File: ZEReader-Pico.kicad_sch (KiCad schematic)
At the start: 0 parts

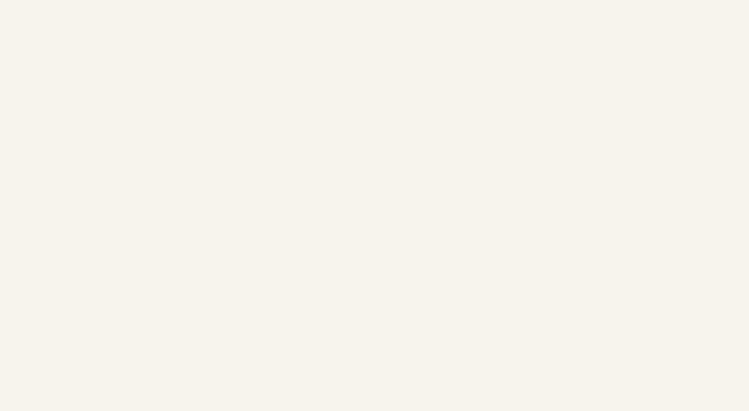
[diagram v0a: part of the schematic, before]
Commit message: Adds SD card connector, control buttons and debug headers
Signed-off-by: Anna-Lena Marx <anna-lena.marx@web.de>
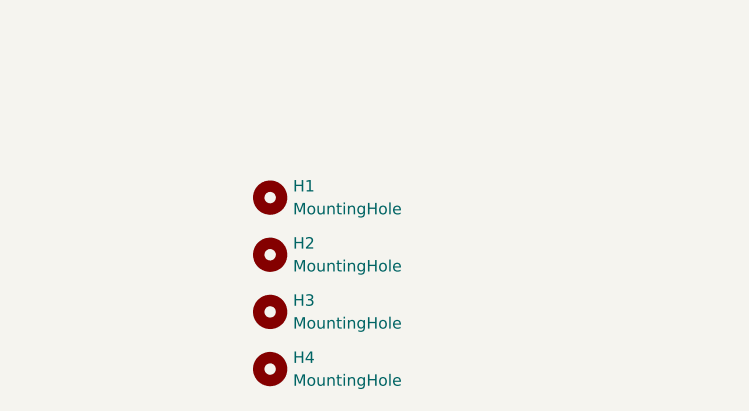
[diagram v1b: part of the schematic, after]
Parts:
- added H1, H2, H3, H4: MountingHole, MountingHole:MountingHole_3.2mm_M3, symbol Mechanical:MountingHole

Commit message: Add EPD Driver Circuit
Signed-off-by: Anna-Lena Marx <anna-lena.marx@web.de>
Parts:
- H1, H2, H3, H4: footprint MountingHole:MountingHole_3.2mm_M3 -> MountingHole:MountingHole_3.2mm_M3_Pad_Via
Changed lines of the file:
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@@
 			)
 		)
-		(property "Footprint" "MountingHole:MountingHole_3.2mm_M3"
+		(property "Footprint" "MountingHole:MountingHole_3.2mm_M3_Pad_Via"
 			(at 78.74 129.54 0)
 			(effects
@@
 			)
 		)
-		(property "Footprint" "MountingHole:MountingHole_3.2mm_M3"
+		(property "Footprint" "MountingHole:MountingHole_3.2mm_M3_Pad_Via"
 			(at 78.74 148.59 0)
 			(effects
@@
 			)
 		)
-		(property "Footprint" "MountingHole:MountingHole_3.2mm_M3"
+		(property "Footprint" "MountingHole:MountingHole_3.2mm_M3_Pad_Via"
 			(at 78.74 142.24 0)
 			(effects
@@
 			)
 		)
-		(property "Footprint" "MountingHole:MountingHole_3.2mm_M3"
+		(property "Footprint" "MountingHole:MountingHole_3.2mm_M3_Pad_Via"
 			(at 78.74 135.89 0)
 			(effects

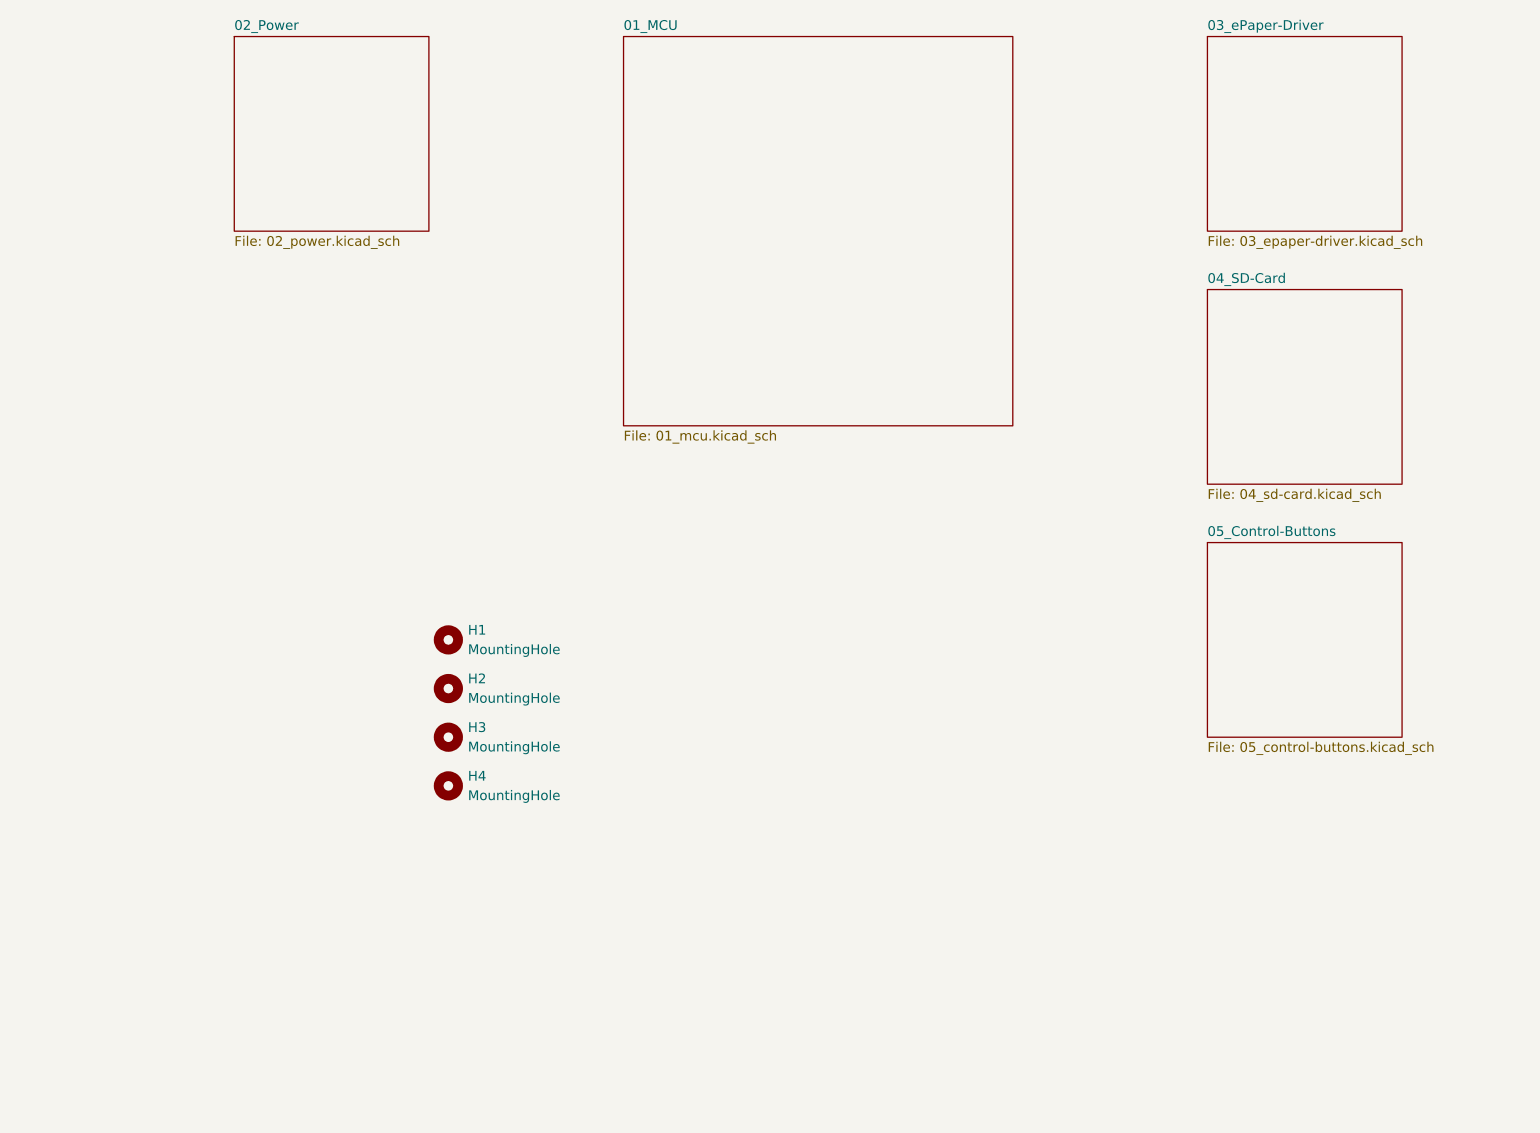
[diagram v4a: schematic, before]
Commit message: Migrate to KiCad 9, start working on the new revision
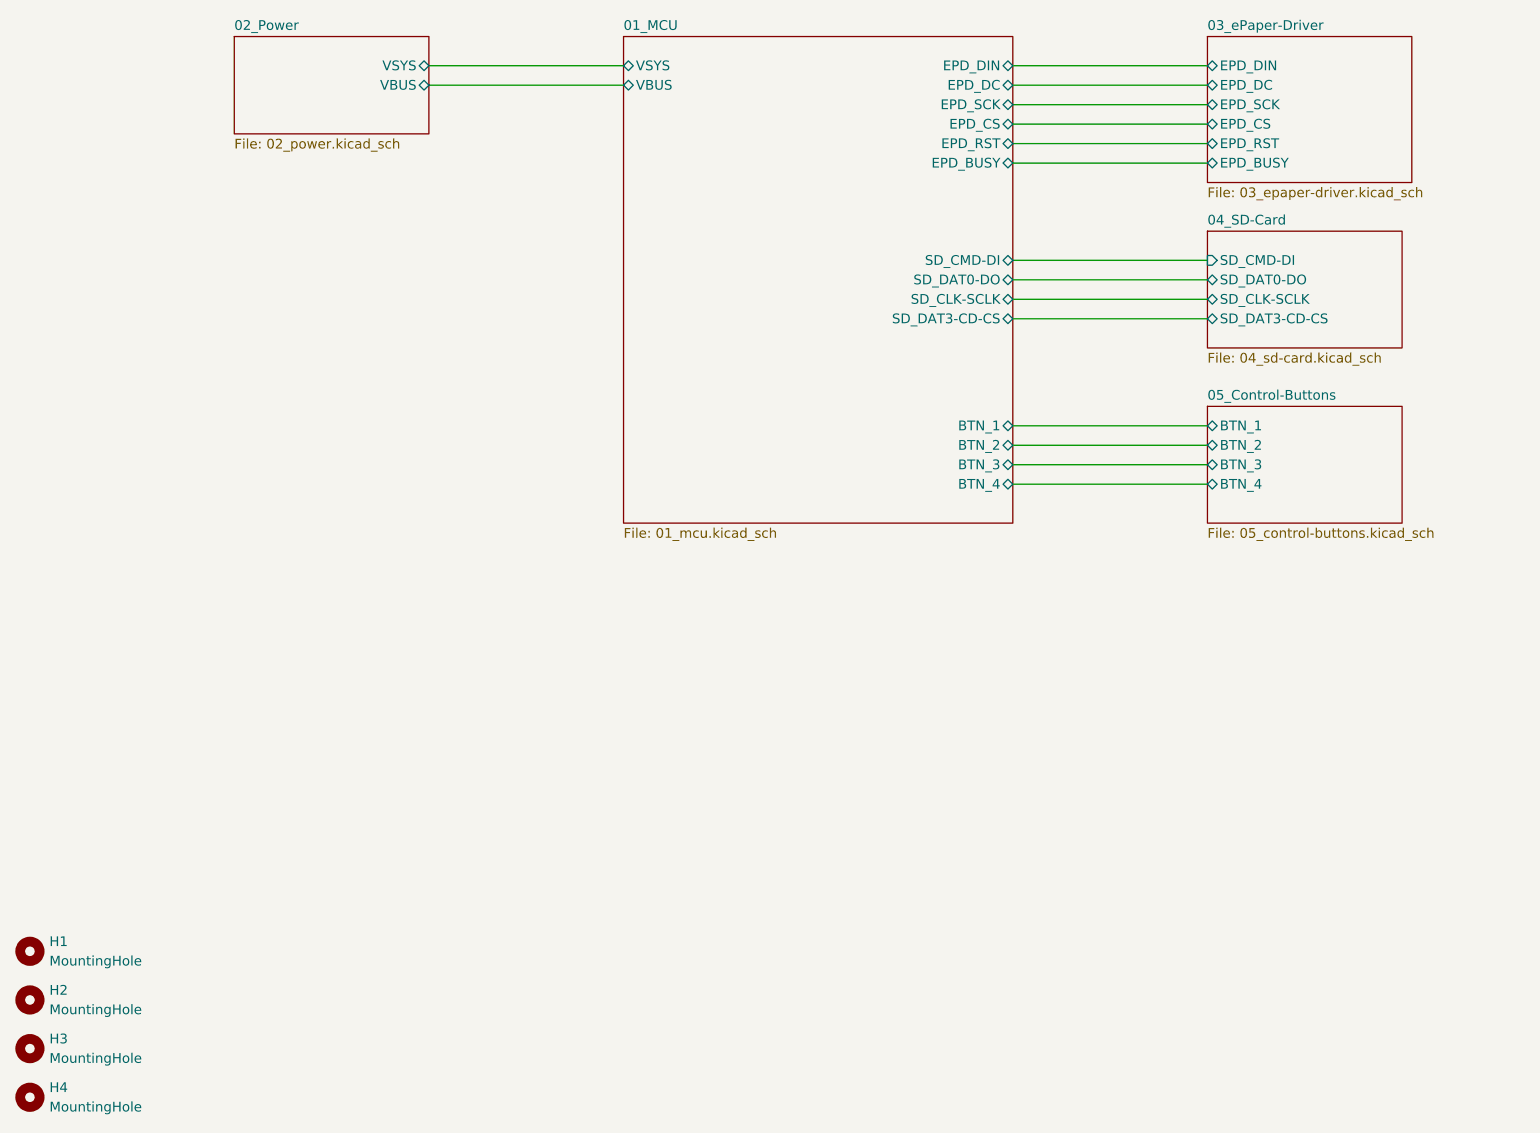
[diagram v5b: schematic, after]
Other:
- sheet 01_MCU ports: added BTN_1, BTN_2, BTN_3, BTN_4, EPD_BUSY, EPD_CS, EPD_DC, EPD_DIN, EPD_RST, EPD_SCK, SD_CLK-SCLK, SD_CMD-DI, SD_DAT0-DO, SD_DAT3-CD-CS, VBUS, VSYS; removed none
- sheet 02_Power ports: added VBUS, VSYS; removed none
- sheet 03_ePaper-Driver ports: added EPD_BUSY, EPD_CS, EPD_DC, EPD_DIN, EPD_RST, EPD_SCK; removed none
- sheet 04_SD-Card ports: added SD_CLK-SCLK, SD_CMD-DI, SD_DAT0-DO, SD_DAT3-CD-CS; removed none
- sheet 05_Control-Buttons ports: added BTN_1, BTN_2, BTN_3, BTN_4; removed none
- moved on the sheet: H1, H2, H3, H4

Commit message: fully connect the sd connector, redraw sd and buttons
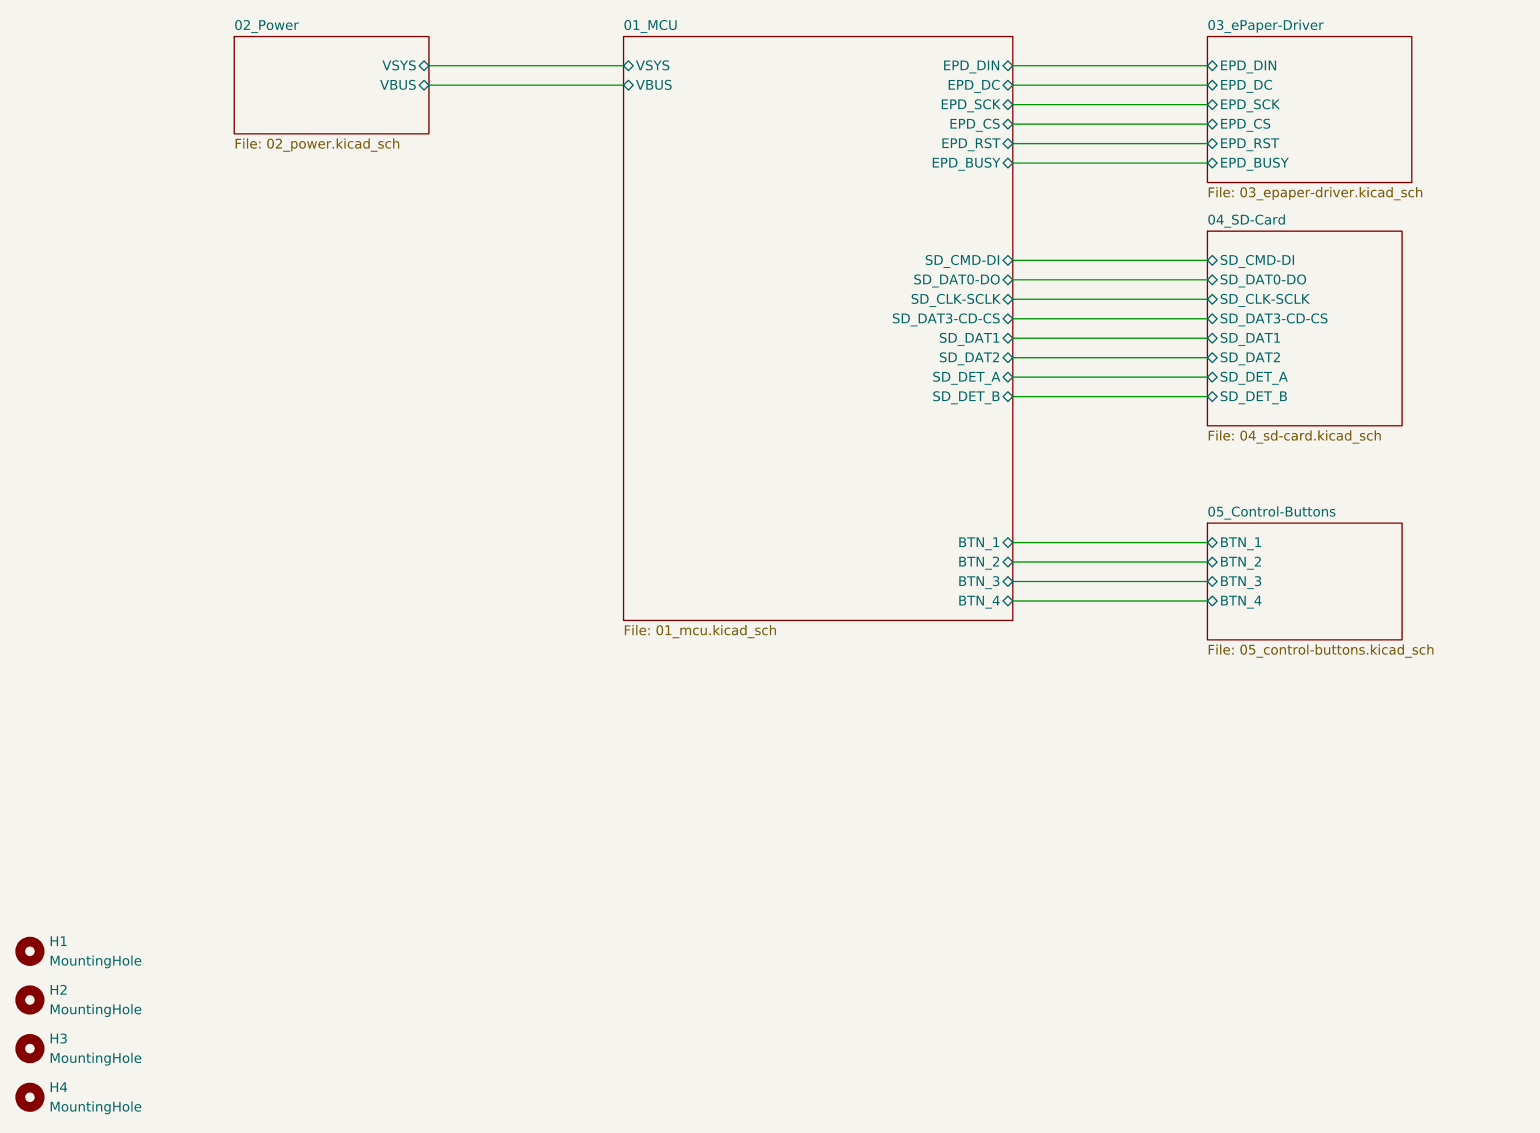
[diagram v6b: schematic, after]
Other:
- sheet 01_MCU ports: added SD_DAT1, SD_DAT2, SD_DET_A, SD_DET_B; removed none
- sheet 04_SD-Card ports: added SD_DAT1, SD_DAT2, SD_DET_A, SD_DET_B; removed none
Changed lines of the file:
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@@
 	(wire
 		(pts
-			(xy 152.4 104.14) (xy 177.8 104.14)
+			(xy 152.4 119.38) (xy 177.8 119.38)
+		)
+		(stroke
+			(width 0)
+			(type default)
+		)
+	)
+	(wire
+		(pts
+			(xy 152.4 90.17) (xy 177.8 90.17)
 		)
 		(stroke
@@
 	(wire
 		(pts
-			(xy 152.4 101.6) (xy 177.8 101.6)
-		)
-		(stroke
-			(width 0)
-			(type default)
-		)
-	)
-	(wire
-		(pts
-			(xy 152.4 109.22) (xy 177.8 109.22)
-		)
-		(stroke
-			(width 0)
-			(type default)
-		)
-	)
-	(wire
-		(pts
-			(xy 152.4 106.68) (xy 177.8 106.68)
+			(xy 152.4 95.25) (xy 177.8 95.25)
+		)
+		(stroke
+			(width 0)
+			(type default)
+		)
+	)
+	(wire
+		(pts
+			(xy 152.4 97.79) (xy 177.8 97.79)
+		)
+		(stroke
+			(width 0)
+			(type default)
+		)
+	)
+	(wire
+		(pts
+			(xy 152.4 116.84) (xy 177.8 116.84)
+		)
+		(stroke
+			(width 0)
+			(type default)
+		)
+	)
+	(wire
+		(pts
+			(xy 152.4 124.46) (xy 177.8 124.46)
+		)
+		(stroke
+			(width 0)
+			(type default)
+		)
+	)
+	(wire
+		(pts
+			(xy 152.4 121.92) (xy 177.8 121.92)
 		)
 		(stroke
@@
 		(pts
 			(xy 152.4 85.09) (xy 177.8 85.09)
+		)
+		(stroke
+			(width 0)
+			(type default)
+		)
+	)
+	(wire
+		(pts
+			(xy 152.4 92.71) (xy 177.8 92.71)
 		)
 		(stroke
@@
 	)
 	(sheet
-		(at 177.8 99.06)
+		(at 177.8 114.3)
 		(size 25.4 15.24)
 		(exclude_from_sim no)
@@
 		)
 		(property "Sheetname" "05_Control-Buttons"
-			(at 177.8 98.3484 0)
+			(at 177.8 113.5884 0)
 			(effects
 				(font
@@
 		)
 		(property "Sheetfile" "05_control-buttons.kicad_sch"
-			(at 177.8 114.8846 0)
+			(at 177.8 130.1246 0)
 			(effects
 				(font
@@
 		)
 		(pin "BTN_1" bidirectional
-			(at 177.8 101.6 180)
+			(at 177.8 116.84 180)
 			(effects
 				(font
@@
 		)
 		(pin "BTN_4" bidirectional
-			(at 177.8 109.22 180)
+			(at 177.8 124.46 180)
 			(effects
 				(font
@@
 		)
 		(pin "BTN_2" bidirectional
-			(at 177.8 104.14 180)
+			(at 177.8 119.38 180)
 			(effects
 				(font
@@
 		)
 		(pin "BTN_3" bidirectional
-			(at 177.8 106.68 180)
+			(at 177.8 121.92 180)
 			(effects
 				(font
@@
 	(sheet
 		(at 177.8 76.2)
-		(size 25.4 15.24)
+		(size 25.4 25.4)
 		(exclude_from_sim no)
 		(in_bom yes)
@@
 		)
 		(property "Sheetfile" "04_sd-card.kicad_sch"
-			(at 177.8 92.0246 0)
+			(at 177.8 102.1846 0)
 			(effects
 				(font
@@
 			)
 		)
-		(pin "SD_CMD-DI" input
-			(at 177.8 80.01 180)
-			(effects
-				(font
-					(size 1.27 1.27)
-				)
-				(justify left)
-			)
-		)
 		(pin "SD_DAT0-DO" bidirectional
 			(at 177.8 82.55 180)
@@
 		(pin "SD_DAT3-CD-CS" bidirectional
 			(at 177.8 87.63 180)
+			(effects
+				(font
+					(size 1.27 1.27)
+				)
+				(justify left)
+			)
+		)
+		(pin "SD_DAT1" bidirectional
+			(at 177.8 90.17 180)
+			(effects
+				(font
+					(size 1.27 1.27)
+				)
+				(justify left)
+			)
+		)
+		(pin "SD_DAT2" bidirectional
+			(at 177.8 92.71 180)
+			(effects
+				(font
+					(size 1.27 1.27)
+				)
+				(justify left)
+			)
+		)
+		(pin "SD_DET_A" bidirectional
+			(at 177.8 95.25 180)
+			(effects
+				(font
+					(size 1.27 1.27)
+				)
+				(justify left)
+			)
+		)
+		(pin "SD_DET_B" bidirectional
+			(at 177.8 97.79 180)
+			(effects
+				(font
+					(size 1.27 1.27)
+				)
+				(justify left)
+			)
+		)
+		(pin "SD_CMD-DI" bidirectional
+			(at 177.8 80.01 180)
 			(effects
 				(font
@@
 	(sheet
 		(at 101.6 50.8)
-		(size 50.8 63.5)
+		(size 50.8 76.2)
 		(exclude_from_sim no)
 		(in_bom yes)
@@
 		)
 		(property "Sheetfile" "01_mcu.kicad_sch"
-			(at 101.6 114.8846 0)
+			(at 101.6 127.5846 0)
 			(effects
 				(font
@@
 		)
 		(pin "BTN_1" bidirectional
-			(at 152.4 101.6 0)
+			(at 152.4 116.84 0)
 			(effects
 				(font
@@
 		)
 		(pin "BTN_2" bidirectional
-			(at 152.4 104.14 0)
+			(at 152.4 119.38 0)
 			(effects
 				(font
@@
 		)
 		(pin "BTN_4" bidirectional
-			(at 152.4 109.22 0)
+			(at 152.4 124.46 0)
 			(effects
 				(font
@@
 		)
 		(pin "BTN_3" bidirectional
-			(at 152.4 106.68 0)
+			(at 152.4 121.92 0)
 			(effects
 				(font
@@
 			(effects
 				(font
+					(size 1.27 1.27)
+				)
+				(justify right)
+			)
+		)
+		(pin "SD_DAT1" bidirectional
+			(at 152.4 90.17 0)
+			(effects
+				(font
+					(size 1.27 1.27)
+				)
+				(justify right)
+			)
+		)
+		(pin "SD_DAT2" bidirectional
+			(at 152.4 92.71 0)
+			(effects
+				(font
+					(size 1.27 1.27)
+				)
+				(justify right)
+			)
+		)
+		(pin "SD_DET_A" bidirectional
+			(at 152.4 95.25 0)
+			(effects
+				(font
+					(size 1.27 1.27)
+				)
+				(justify right)
+			)
+		)
+		(pin "SD_DET_B" bidirectional
+			(at 152.4 97.79 0)
+			(effects
+				(font

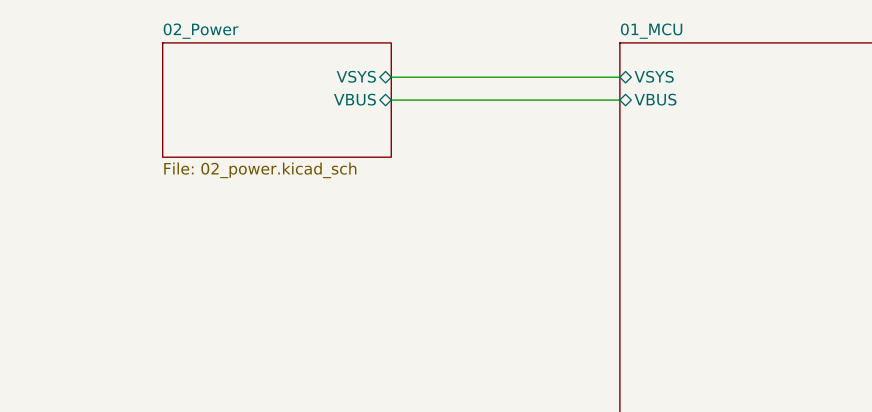
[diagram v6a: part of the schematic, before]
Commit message: updated power path, connect USB-C to pico's USB data
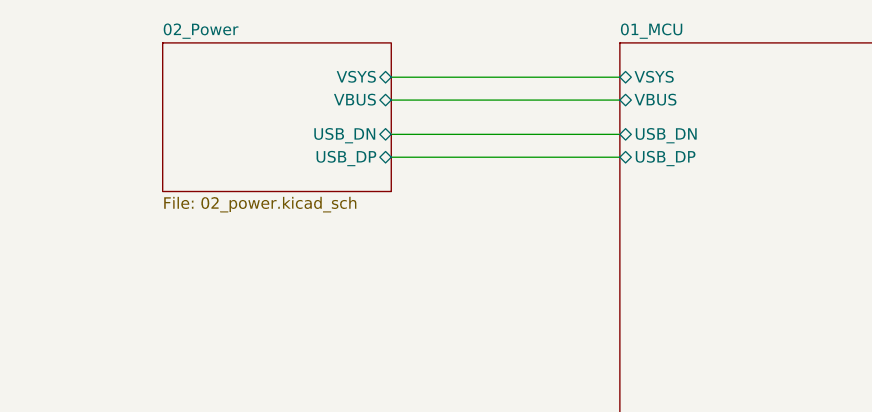
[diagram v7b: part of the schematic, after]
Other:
- sheet 01_MCU ports: added USB_DN, USB_DP; removed none
- sheet 02_Power ports: added USB_DN, USB_DP; removed none
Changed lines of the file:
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@@
+	(wire
+		(pts
+			(xy 76.2 63.5) (xy 101.6 63.5)
+		)
+		(stroke
+			(width 0)
+			(type default)
+		)
+	)
 	(wire
 		(pts
@@
 		(pts
 			(xy 152.4 82.55) (xy 177.8 82.55)
+		)
+		(stroke
+			(width 0)
+			(type default)
+		)
+	)
+	(wire
+		(pts
+			(xy 76.2 60.96) (xy 101.6 60.96)
 		)
 		(stroke
@@
 			)
 		)
+		(pin "USB_DP" bidirectional
+			(at 101.6 63.5 180)
+			(effects
+				(font
+					(size 1.27 1.27)
+				)
+				(justify left)
+			)
+		)
+		(pin "USB_DN" bidirectional
+			(at 101.6 60.96 180)
+			(effects
+				(font
+					(size 1.27 1.27)
+				)
+				(justify left)
+			)
+		)
 		(instances
 			(project "ZEReader-Pico"
@@
 	(sheet
 		(at 50.8 50.8)
-		(size 25.4 12.7)
+		(size 25.4 16.51)
 		(exclude_from_sim no)
 		(in_bom yes)
@@
 		)
 		(property "Sheetfile" "02_power.kicad_sch"
-			(at 50.8 64.0846 0)
+			(at 50.8 67.8946 0)
 			(effects
 				(font
@@
 			(effects
 				(font
+					(size 1.27 1.27)
+				)
+				(justify right)
+			)
+		)
+		(pin "USB_DN" bidirectional
+			(at 76.2 60.96 0)
+			(effects
+				(font
+					(size 1.27 1.27)
+				)
+				(justify right)
+			)
+		)
+		(pin "USB_DP" bidirectional
+			(at 76.2 63.5 0)
+			(effects
+				(font
